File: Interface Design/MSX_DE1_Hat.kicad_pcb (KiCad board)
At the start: 2 copper layers, 103 x 66 mm, 26 parts, among them J1 J1, J2 J2, J3 J3, J4 J4, J5 J5, J6 J6, U1 74LVC245A, U2 74LVC245A, U3 74LVC245A, U4 74LVC245A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

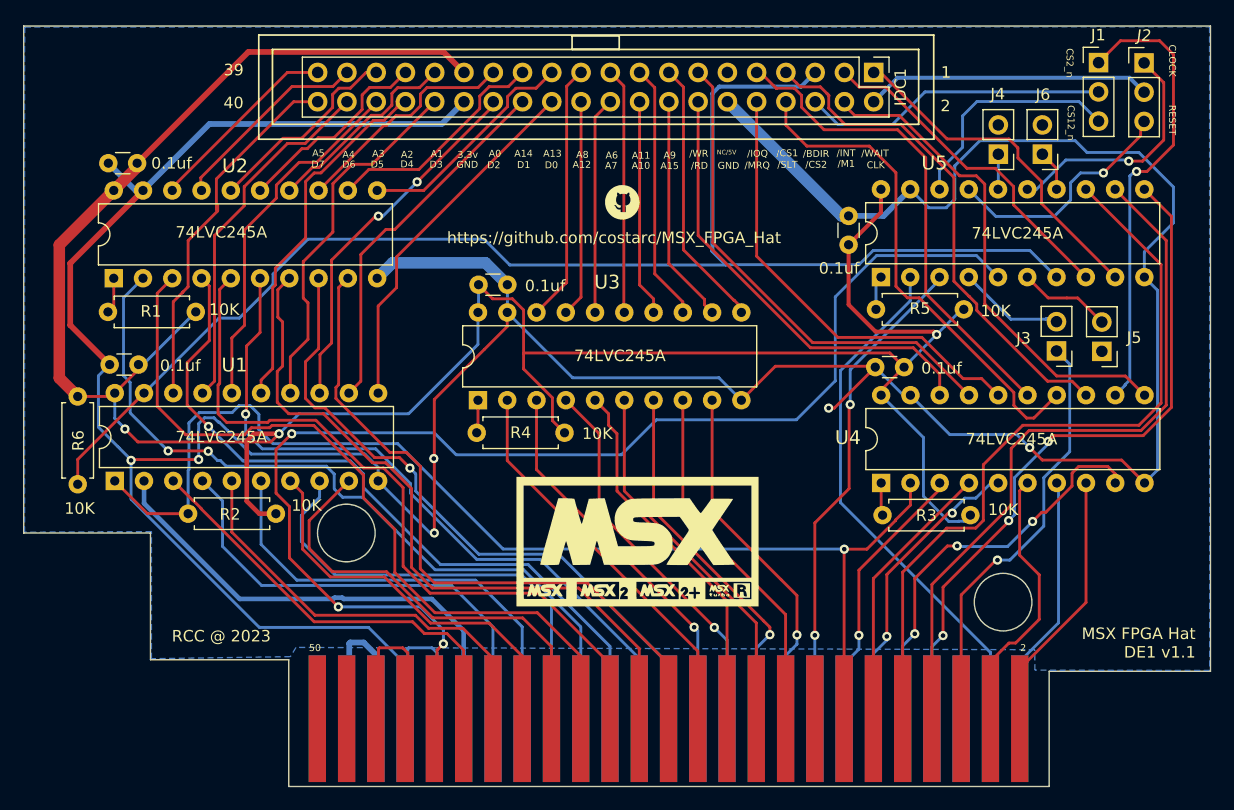
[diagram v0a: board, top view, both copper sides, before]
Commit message: Compatibel with DE0 & DE1
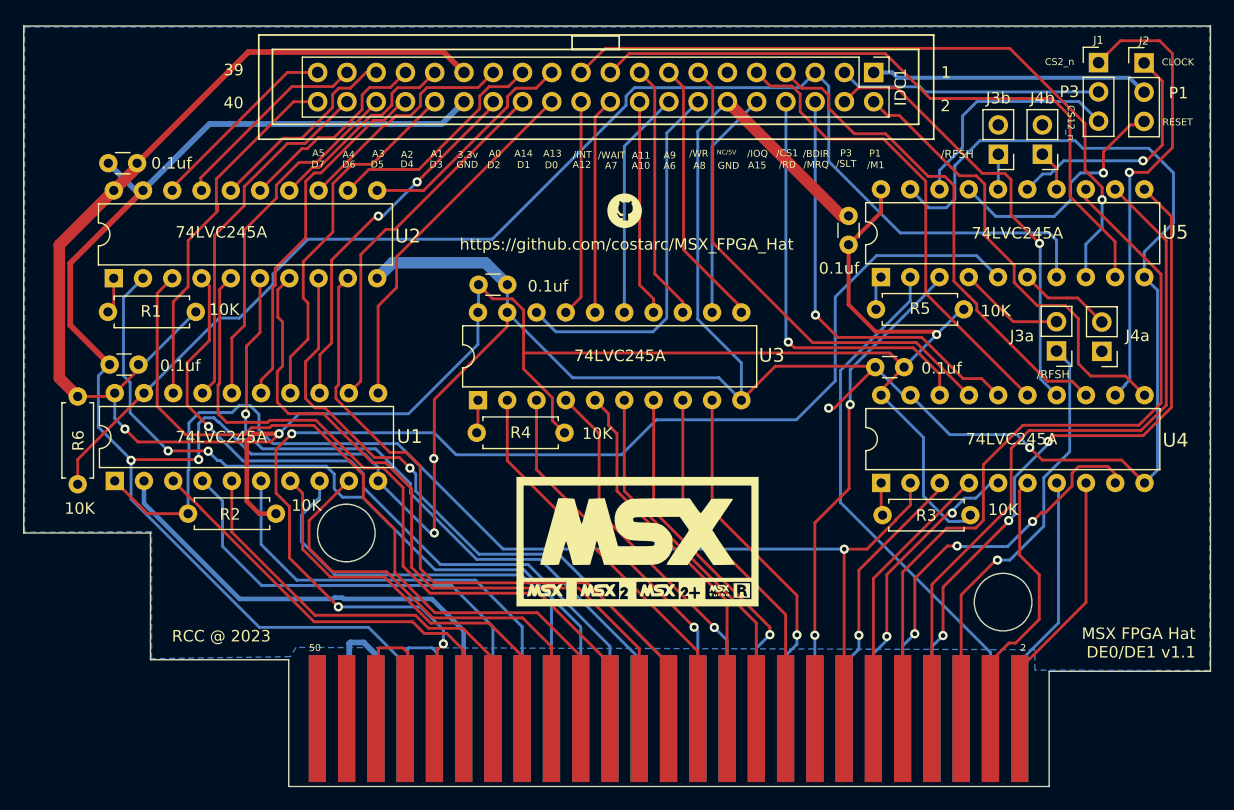
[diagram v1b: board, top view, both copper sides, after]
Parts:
- J3a1: renamed from J3; value J3 -> J3a
- J3b1: renamed from J4; value J4 -> J3b
- J4a1: renamed from J5; value J5 -> J4a
- J4b1: renamed from J6; value J6 -> J4b
- moved G*** 0.76 mm to (104.1, 36.2)
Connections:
- IDC1 pad 1: /C_WAIT -> C_CLK_OR_RST
- IDC1 pad 10: /C_MREQ -> C_A15
- IDC1 pad 14: /C_RD -> C_A8
- IDC1 pad 16: C_A15 -> C_A6
- IDC1 pad 19: C_A6 -> /C_WAIT
- IDC1 pad 2: C_CLK_OR_RST -> /C_M1
- IDC1 pad 21: C_A8 -> /C_INT
- IDC1 pad 3: /C_INT -> C_CS2_CS12
- IDC1 pad 4: /C_M1 -> /C_SLTSL
- IDC1 pad 6: C_CS2_CS12 -> /C_MREQ
- IDC1 pad 8: /C_SLTSL -> /C_RD
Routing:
- net /C_INT: track 29.2 -> 61.8 mm, vias 0 -> 1
- net /C_WAIT: track 29.9 -> 58.4 mm
- net GNDREF: track 335.4 -> 358.4 mm
- net C_A8: track 22.6 -> 32.4 mm
- net /C_BUSDIR: track 123.0 -> 115.1 mm
- net /C_SLTSL: track 43.3 -> 38.6 mm, vias 0 -> 1
- net C_CS2_CS12: track 26.6 -> 22.8 mm
- net /C_M1: track 42.9 -> 39.9 mm
- net /C_RD: track 39.4 -> 37.1 mm, vias 0 -> 1
- net /C_MREQ: track 39.4 -> 37.1 mm, vias 0 -> 1
- net C_A6: track 21.3 -> 19.9 mm
- net /C_IORQ: track 42.6 -> 41.7 mm
- net C_CLK_OR_RST: track 24.8 -> 24.2 mm
- net /C_RESET: track 21.0 -> 21.6 mm
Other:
- board text added: "/RFSH"
- board text added: "MSX FPGA Hat DE0/DE1 v1.1"
- board text added: "P1"
- board text added: "P3"
- board text removed: "/CS2"
- board text removed: "CLK"
- board text removed: "MSX FPGA Hat DE1 v1.1"
